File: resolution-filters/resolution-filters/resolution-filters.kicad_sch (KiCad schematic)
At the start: 55 parts, among them J501 Conn_Coaxial, J502 Terminal Block, J503 Conn_Coaxial, K501 G5V-1, K502 G5V-1, SW501 SW_SPST, T501 Transformer_1P_1S, T502 Transformer_1P_1S, Y501 Crystal_GND3_Small, Y502 Crystal_GND3_Small, Y503 Crystal_GND3_Small, Y504 Crystal_GND3_Small

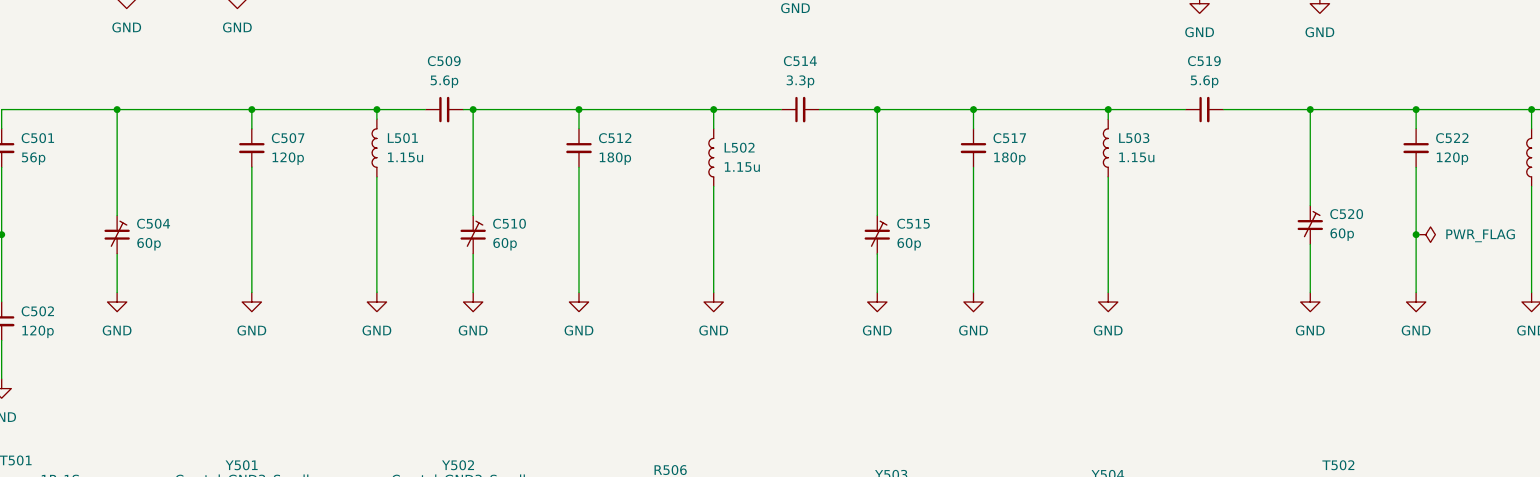
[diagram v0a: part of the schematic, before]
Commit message: updates to if log amp and resolution filter boards
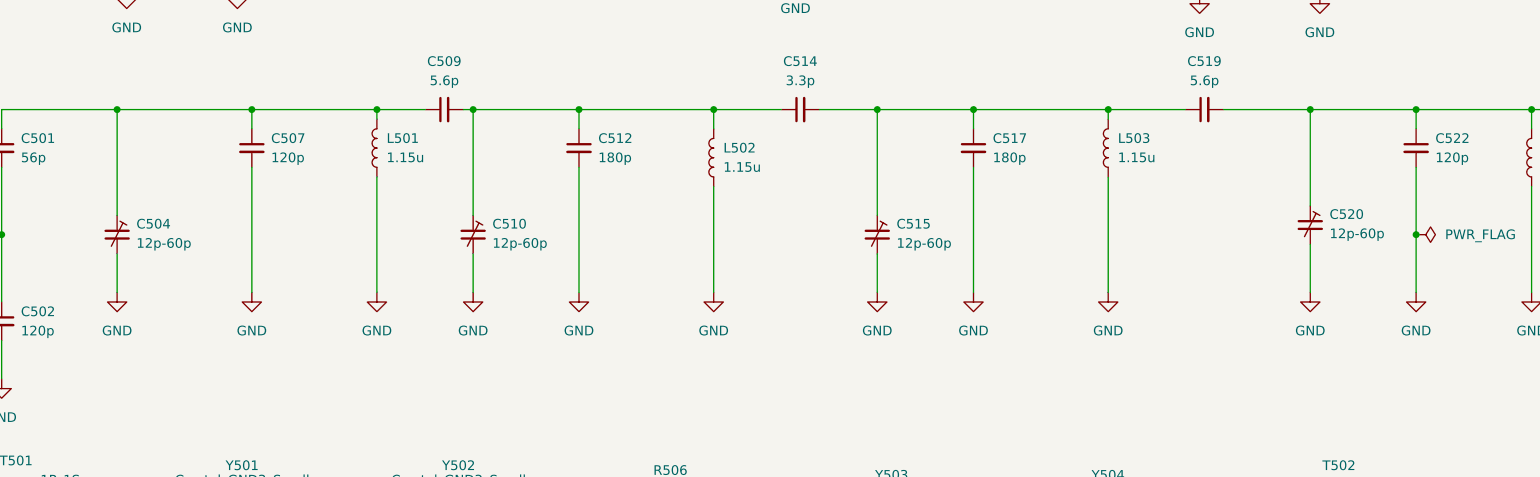
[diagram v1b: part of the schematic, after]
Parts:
- C504, C510, C515, C520: value 60p -> 12p-60p
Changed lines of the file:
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@@
       (effects (font (size 1.27 1.27)) (justify left))
     )
-    (property "Value" "60p" (id 1) (at 213.36 77.9779 0)
+    (property "Value" "12p-60p" (id 1) (at 213.36 77.9779 0)
       (effects (font (size 1.27 1.27)) (justify left))
     )
@@
       (effects (font (size 1.27 1.27)) hide)
     )
-    (property "Datasheet" "~" (id 3) (at 210.82 76.835 0)
+    (property "Datasheet" "https://media.digikey.com/pdf/Data%20Sheets/EW%20Electronics-Edmar/GKGxx015_016_Series_DS.pdf" (id 3) (at 210.82 76.835 0)
       (effects (font (size 1.27 1.27)) hide)
     )
@@
       (effects (font (size 1.27 1.27)) (justify left))
     )
-    (property "Value" "60p" (id 1) (at 55.88 79.2479 0)
+    (property "Value" "12p-60p" (id 1) (at 55.88 79.2479 0)
       (effects (font (size 1.27 1.27)) (justify left))
     )
@@
       (effects (font (size 1.27 1.27)) hide)
     )
-    (property "Datasheet" "~" (id 3) (at 53.34 78.105 0)
+    (property "Datasheet" "https://media.digikey.com/pdf/Data%20Sheets/EW%20Electronics-Edmar/GKGxx015_016_Series_DS.pdf" (id 3) (at 53.34 78.105 0)
       (effects (font (size 1.27 1.27)) hide)
     )
@@
       (effects (font (size 1.27 1.27)) hide)
     )
-    (property "Datasheet" "~" (id 3) (at 80.01 118.11 0)
+    (property "Datasheet" "https://media.digikey.com/pdf/Data%20Sheets/EW%20Electronics-Edmar/GKGxx015_016_Series_DS.pdf" (id 3) (at 80.01 118.11 0)
       (effects (font (size 1.27 1.27)) hide)
     )
@@
       (effects (font (size 1.27 1.27)) (justify left))
     )
-    (property "Value" "60p" (id 1) (at 156.21 79.2479 0)
+    (property "Value" "12p-60p" (id 1) (at 156.21 79.2479 0)
       (effects (font (size 1.27 1.27)) (justify left))
     )
@@
       (effects (font (size 1.27 1.27)) hide)
     )
-    (property "Datasheet" "~" (id 3) (at 153.67 78.105 0)
+    (property "Datasheet" "https://media.digikey.com/pdf/Data%20Sheets/EW%20Electronics-Edmar/GKGxx015_016_Series_DS.pdf" (id 3) (at 153.67 78.105 0)
       (effects (font (size 1.27 1.27)) hide)
     )
@@
       (effects (font (size 1.27 1.27)) hide)
     )
-    (property "Datasheet" "~" (id 3) (at 53.975 118.11 0)
+    (property "Datasheet" "https://media.digikey.com/pdf/Data%20Sheets/EW%20Electronics-Edmar/GKGxx015_016_Series_DS.pdf" (id 3) (at 53.975 118.11 0)
       (effects (font (size 1.27 1.27)) hide)
     )
@@
       (effects (font (size 1.27 1.27)) hide)
     )
-    (property "Datasheet" "~" (id 3) (at 139.7 118.11 0)
+    (property "Datasheet" "https://media.digikey.com/pdf/Data%20Sheets/EW%20Electronics-Edmar/GKGxx015_016_Series_DS.pdf" (id 3) (at 139.7 118.11 0)
       (effects (font (size 1.27 1.27)) hide)
     )
@@
       (effects (font (size 1.27 1.27)) hide)
     )
-    (property "Datasheet" "~" (id 3) (at 108.585 118.11 0)
+    (property "Datasheet" "https://media.digikey.com/pdf/Data%20Sheets/EW%20Electronics-Edmar/GKGxx015_016_Series_DS.pdf" (id 3) (at 108.585 118.11 0)
       (effects (font (size 1.27 1.27)) hide)
     )
@@
       (effects (font (size 1.27 1.27)) (justify left))
     )
-    (property "Value" "60p" (id 1) (at 102.87 79.2479 0)
+    (property "Value" "12p-60p" (id 1) (at 102.87 79.2479 0)
       (effects (font (size 1.27 1.27)) (justify left))
     )
@@
       (effects (font (size 1.27 1.27)) hide)
     )
-    (property "Datasheet" "~" (id 3) (at 100.33 78.105 0)
+    (property "Datasheet" "https://media.digikey.com/pdf/Data%20Sheets/EW%20Electronics-Edmar/GKGxx015_016_Series_DS.pdf" (id 3) (at 100.33 78.105 0)
       (effects (font (size 1.27 1.27)) hide)
     )
@@
       (effects (font (size 1.27 1.27)) hide)
     )
-    (property "Datasheet" "~" (id 3) (at 165.735 118.11 0)
+    (property "Datasheet" "https://media.digikey.com/pdf/Data%20Sheets/EW%20Electronics-Edmar/GKGxx015_016_Series_DS.pdf" (id 3) (at 165.735 118.11 0)
       (effects (font (size 1.27 1.27)) hide)
     )
@@
       (effects (font (size 1.27 1.27)) hide)
     )
-    (property "Datasheet" "~" (id 3) (at 194.31 118.11 0)
+    (property "Datasheet" "https://media.digikey.com/pdf/Data%20Sheets/EW%20Electronics-Edmar/GKGxx015_016_Series_DS.pdf" (id 3) (at 194.31 118.11 0)
       (effects (font (size 1.27 1.27)) hide)
     )
@@
     )
     (path "/36e783d5-9ae1-4da1-b87d-c4c3d6925974"
-      (reference "C504") (unit 1) (value "60p") (footprint "resolution-filters:GKG60015")
+      (reference "C504") (unit 1) (value "12p-60p") (footprint "resolution-filters:GKG60015")
     )
     (path "/4bec1a9e-d426-40c2-9e19-6f55ab399553"
@@
     )
     (path "/b2d57885-8786-4dc3-b1c7-b1b397afb79f"
-      (reference "C510") (unit 1) (value "60p") (footprint "resolution-filters:GKG60015")
+      (reference "C510") (unit 1) (value "12p-60p") (footprint "resolution-filters:GKG60015")
     )
     (path "/6fde542f-7e50-4e51-af22-5524655c45fa"
@@
     )
     (path "/44359aa3-a146-4361-a6d3-bf8baf4d0769"
-      (reference "C515") (unit 1) (value "60p") (footprint "resolution-filters:GKG60015")
+      (reference "C515") (unit 1) (value "12p-60p") (footprint "resolution-filters:GKG60015")
     )
     (path "/bb468ebc-7f2d-418e-96a5-492d38be3103"
@@
     )
     (path "/086ca953-977d-4699-95a4-445af35df2d6"
-      (reference "C520") (unit 1) (value "60p") (footprint "resolution-filters:GKG60015")
+      (reference "C520") (unit 1) (value "12p-60p") (footprint "resolution-filters:GKG60015")
     )
     (path "/0b86b0d9-0bc7-476e-8171-fcb06edd78e3"

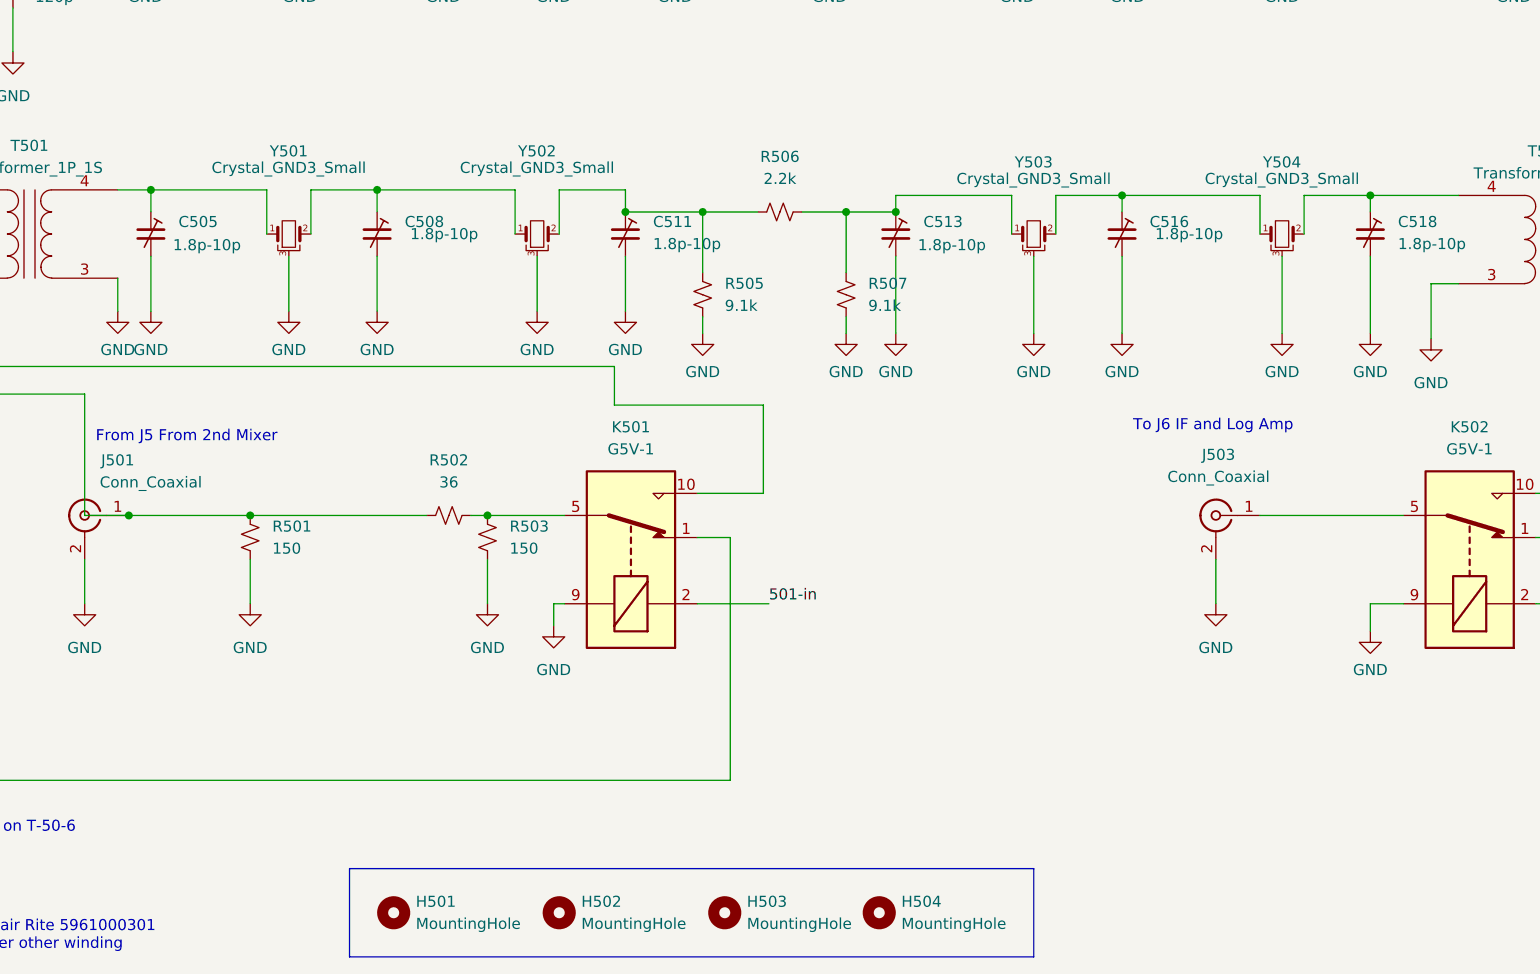
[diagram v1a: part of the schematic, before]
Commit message: fix transformer issue
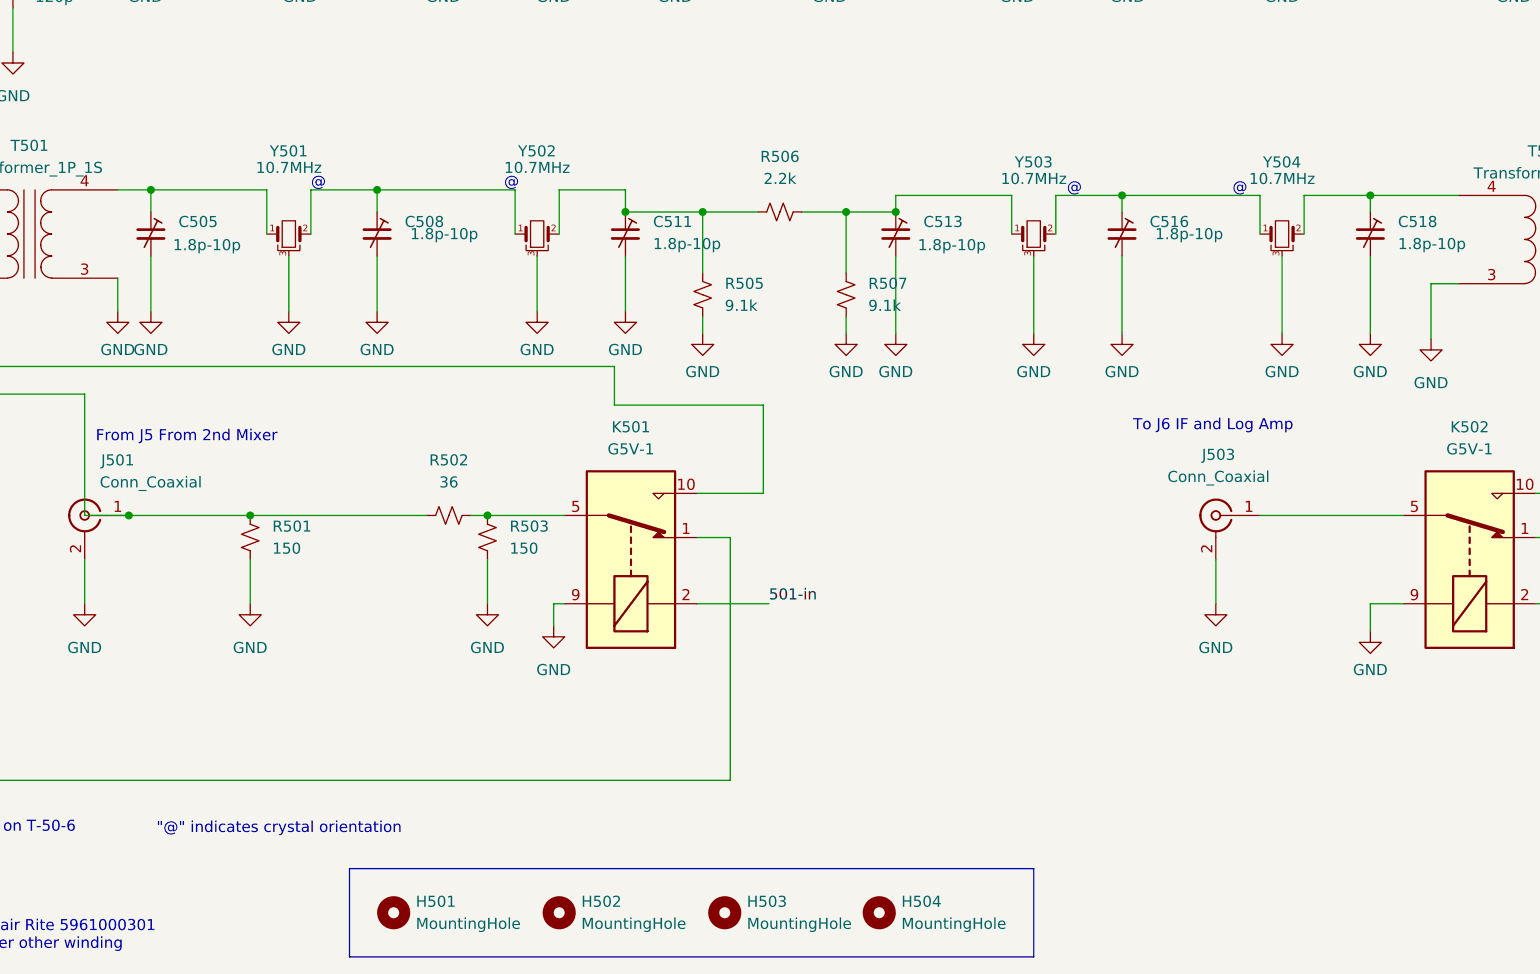
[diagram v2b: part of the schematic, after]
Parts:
- T501, T502: footprint Inductor_THT:L_Toroid_Vertical_L13.0mm_W6.5mm_P5.60mm -> Transformer_THT:Transformer_Toroid_Horizontal_D14.0mm_Amidon-T50
- Y501, Y502, Y503, Y504: value Crystal_GND3_Small -> 10.7MHz
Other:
- note added: ""@" indicates crystal orientation"
- note added: "@"
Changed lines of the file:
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@@
     (stroke (width 0) (type default) (color 0 0 0 0))
+  )
+  (text "@" (at 178.435 113.665 0)
+    (effects (font (size 1.27 1.27)) (justify left bottom))
   )
   (text "Transformers:\n39 turns #30 wire on\nAmidon FT-50-61 or Fair Rite 5961000301\nLink = 5turns #24 over other winding"
@@
     (effects (font (size 1.27 1.27)) (justify left bottom))
   )
+  (text "@" (at 159.385 113.665 0)
+    (effects (font (size 1.27 1.27)) (justify left bottom))
+  )
   (text "To J6 IF and Log Amp" (at 167.005 140.97 0)
+    (effects (font (size 1.27 1.27)) (justify left bottom))
+  )
+  (text "\"@\" indicates crystal orientation" (at 54.61 187.325 0)
+    (effects (font (size 1.27 1.27)) (justify left bottom))
+  )
+  (text "@" (at 94.615 113.03 0)
+    (effects (font (size 1.27 1.27)) (justify left bottom))
+  )
+  (text "@" (at 72.39 113.03 0)
     (effects (font (size 1.27 1.27)) (justify left bottom))
   )
@@
     (property "Reference" "T502" (id 0) (at 214.6173 108.585 0))
     (property "Value" "Transformer_1P_1S" (id 1) (at 214.6173 111.125 0))
-    (property "Footprint" "Inductor_THT:L_Toroid_Vertical_L13.0mm_W6.5mm_P5.60mm" (id 2) (at 214.63 118.745 0)
+    (property "Footprint" "Transformer_THT:Transformer_Toroid_Horizontal_D14.0mm_Amidon-T50" (id 2) (at 214.63 118.745 0)
       (effects (font (size 1.27 1.27)) hide)
     )
@@
     (in_bom yes) (on_board yes)
     (property "Reference" "Y503" (id 0) (at 155.575 109.855 0))
-    (property "Value" "Crystal_GND3_Small" (id 1) (at 155.575 111.76 0))
+    (property "Value" "10.7MHz" (id 1) (at 155.575 111.76 0))
     (property "Footprint" "resolution-filters:XTAL_ECS-10.7-7.5B" (id 2) (at 155.575 118.11 0)
       (effects (font (size 1.27 1.27)) hide)
     )
-    (property "Datasheet" "~" (id 3) (at 155.575 118.11 0)
+    (property "Datasheet" "https://www.digikey.com/en/products/detail/ecs-inc/ECS-10-7-7-5B/110031" (id 3) (at 155.575 118.11 0)
       (effects (font (size 1.27 1.27)) hide)
     )
@@
     (property "Reference" "T501" (id 0) (at 40.0177 107.95 0))
     (property "Value" "Transformer_1P_1S" (id 1) (at 40.0177 110.49 0))
-    (property "Footprint" "Inductor_THT:L_Toroid_Vertical_L13.0mm_W6.5mm_P5.60mm" (id 2) (at 40.005 118.11 0)
+    (property "Footprint" "Transformer_THT:Transformer_Toroid_Horizontal_D14.0mm_Amidon-T50" (id 2) (at 40.005 118.11 0)
       (effects (font (size 1.27 1.27)) hide)
     )
@@
     (in_bom yes) (on_board yes)
     (property "Reference" "Y504" (id 0) (at 184.15 109.855 0))
-    (property "Value" "Crystal_GND3_Small" (id 1) (at 184.15 111.76 0))
+    (property "Value" "10.7MHz" (id 1) (at 184.15 111.76 0))
     (property "Footprint" "resolution-filters:XTAL_ECS-10.7-7.5B" (id 2) (at 184.15 118.11 0)
       (effects (font (size 1.27 1.27)) hide)
     )
-    (property "Datasheet" "~" (id 3) (at 184.15 118.11 0)
+    (property "Datasheet" "https://www.digikey.com/en/products/detail/ecs-inc/ECS-10-7-7-5B/110031" (id 3) (at 184.15 118.11 0)
       (effects (font (size 1.27 1.27)) hide)
     )
@@
     (in_bom yes) (on_board yes)
     (property "Reference" "Y502" (id 0) (at 98.425 108.585 0))
-    (property "Value" "Crystal_GND3_Small" (id 1) (at 98.425 110.49 0))
+    (property "Value" "10.7MHz" (id 1) (at 98.425 110.49 0))
     (property "Footprint" "resolution-filters:XTAL_ECS-10.7-7.5B" (id 2) (at 98.425 118.11 0)
       (effects (font (size 1.27 1.27)) hide)
     )
-    (property "Datasheet" "~" (id 3) (at 98.425 118.11 0)
+    (property "Datasheet" "https://www.digikey.com/en/products/detail/ecs-inc/ECS-10-7-7-5B/110031" (id 3) (at 98.425 118.11 0)
       (effects (font (size 1.27 1.27)) hide)
     )
@@
     (in_bom yes) (on_board yes)
     (property "Reference" "Y501" (id 0) (at 69.85 108.585 0))
-    (property "Value" "Crystal_GND3_Small" (id 1) (at 69.85 110.49 0))
+    (property "Value" "10.7MHz" (id 1) (at 69.85 110.49 0))
     (property "Footprint" "resolution-filters:XTAL_ECS-10.7-7.5B" (id 2) (at 69.85 118.11 0)
       (effects (font (size 1.27 1.27)) hide)
     )
-    (property "Datasheet" "~" (id 3) (at 69.85 118.11 0)
+    (property "Datasheet" "https://www.digikey.com/en/products/detail/ecs-inc/ECS-10-7-7-5B/110031" (id 3) (at 69.85 118.11 0)
       (effects (font (size 1.27 1.27)) hide)
     )
@@
     )
     (path "/75587f76-bb6c-4ecd-8497-ab801c1dd625"
-      (reference "T501") (unit 1) (value "Transformer_1P_1S") (footprint "Inductor_THT:L_Toroid_Vertical_L13.0mm_W6.5mm_P5.60mm")
+      (reference "T501") (unit 1) (value "Transformer_1P_1S") (footprint "Transformer_THT:Transformer_Toroid_Horizontal_D14.0mm_Amidon-T50")
     )
     (path "/07ac3fad-8f3c-4068-ae53-91e4dc181eee"
-      (reference "T502") (unit 1) (value "Transformer_1P_1S") (footprint "Inductor_THT:L_Toroid_Vertical_L13.0mm_W6.5mm_P5.60mm")
+      (reference "T502") (unit 1) (value "Transformer_1P_1S") (footprint "Transformer_THT:Transformer_Toroid_Horizontal_D14.0mm_Amidon-T50")
     )
     (path "/95c07863-759b-434d-bbc4-10e35dd940f5"
@@
     )
     (path "/c824767b-ca57-4867-8527-11815d916e34"
-      (reference "Y501") (unit 1) (value "Crystal_GND3_Small") (footprint "resolution-filters:XTAL_ECS-10.7-7.5B")
+      (reference "Y501") (unit 1) (value "10.7MHz") (footprint "resolution-filters:XTAL_ECS-10.7-7.5B")
     )
     (path "/bc3d74aa-5dd6-4810-9c52-54a38394b60f"
-      (reference "Y502") (unit 1) (value "Crystal_GND3_Small") (footprint "resolution-filters:XTAL_ECS-10.7-7.5B")
+      (reference "Y502") (unit 1) (value "10.7MHz") (footprint "resolution-filters:XTAL_ECS-10.7-7.5B")
     )
     (path "/6b38ab15-9442-4590-ab10-2c3a4f73b0f0"
-      (reference "Y503") (unit 1) (value "Crystal_GND3_Small") (footprint "resolution-filters:XTAL_ECS-10.7-7.5B")
+      (reference "Y503") (unit 1) (value "10.7MHz") (footprint "resolution-filters:XTAL_ECS-10.7-7.5B")
     )
     (path "/8c96d15b-2a9a-4bfe-ac9e-af0b6bde75a3"
-      (reference "Y504") (unit 1) (value "Crystal_GND3_Small") (footprint "resolution-filters:XTAL_ECS-10.7-7.5B")
-    )
-  )
+      (reference "Y504") (unit 1) (value "10.7MHz") (footprint "resolution-filters:XTAL_ECS-10.7-7.5B")
+    )
+  )
